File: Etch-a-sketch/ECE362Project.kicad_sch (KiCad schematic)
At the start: 1 part

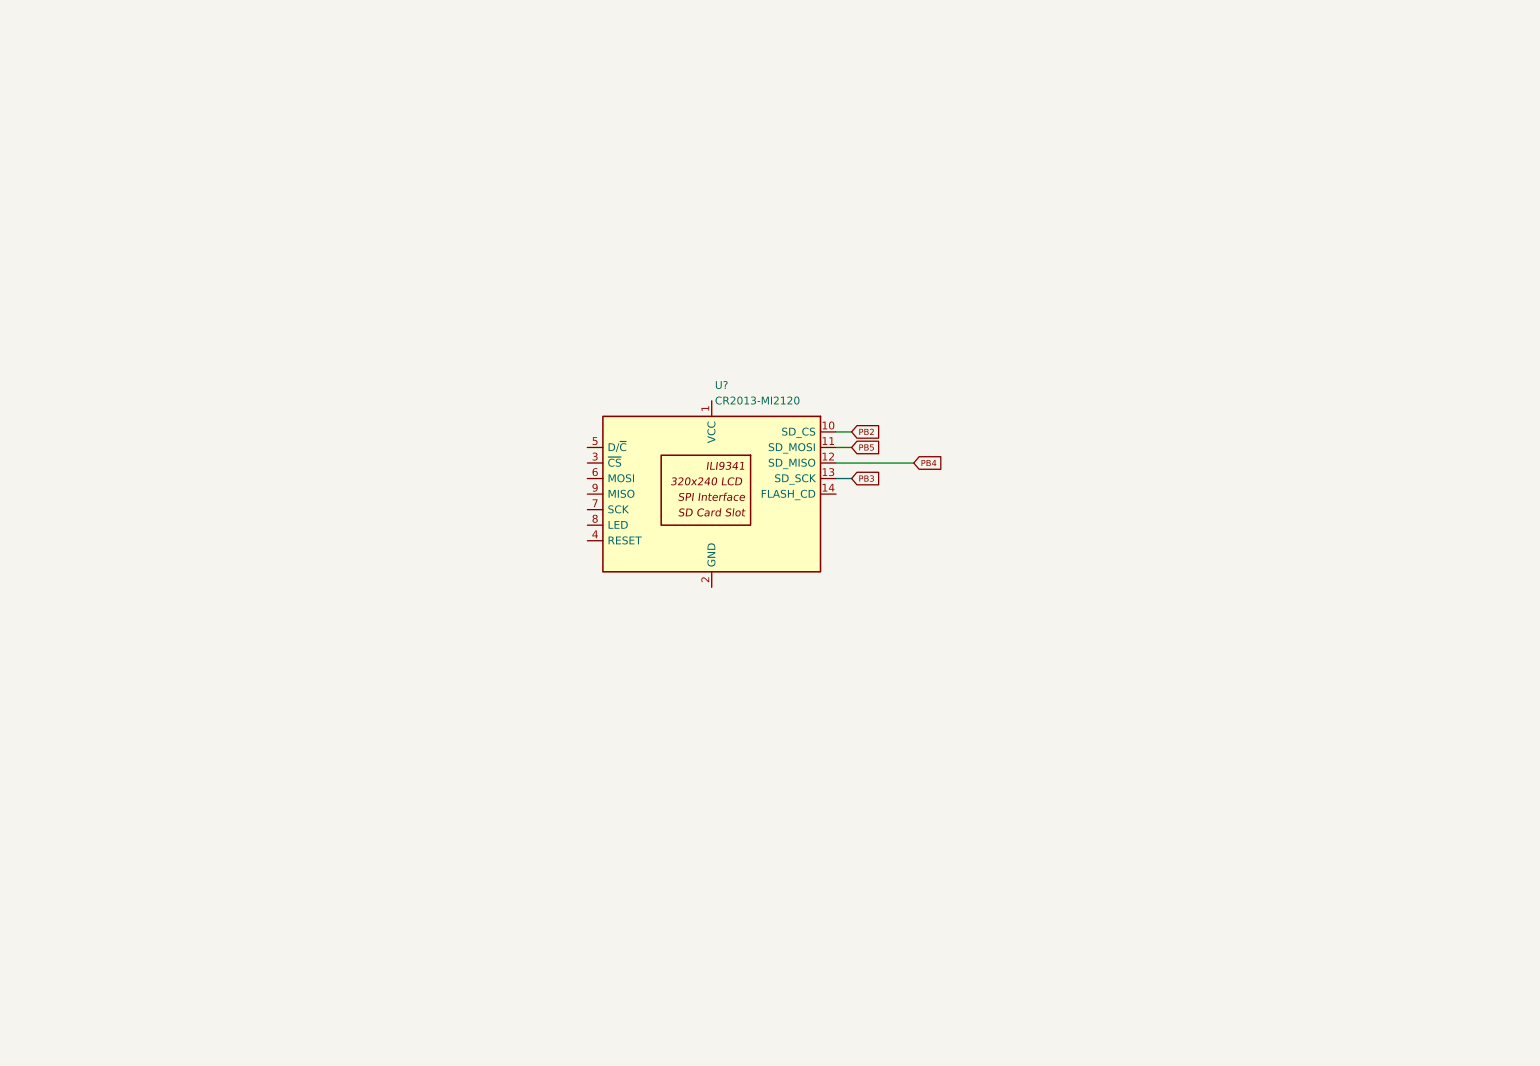
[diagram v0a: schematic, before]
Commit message: finished schematic, should do a schematic review
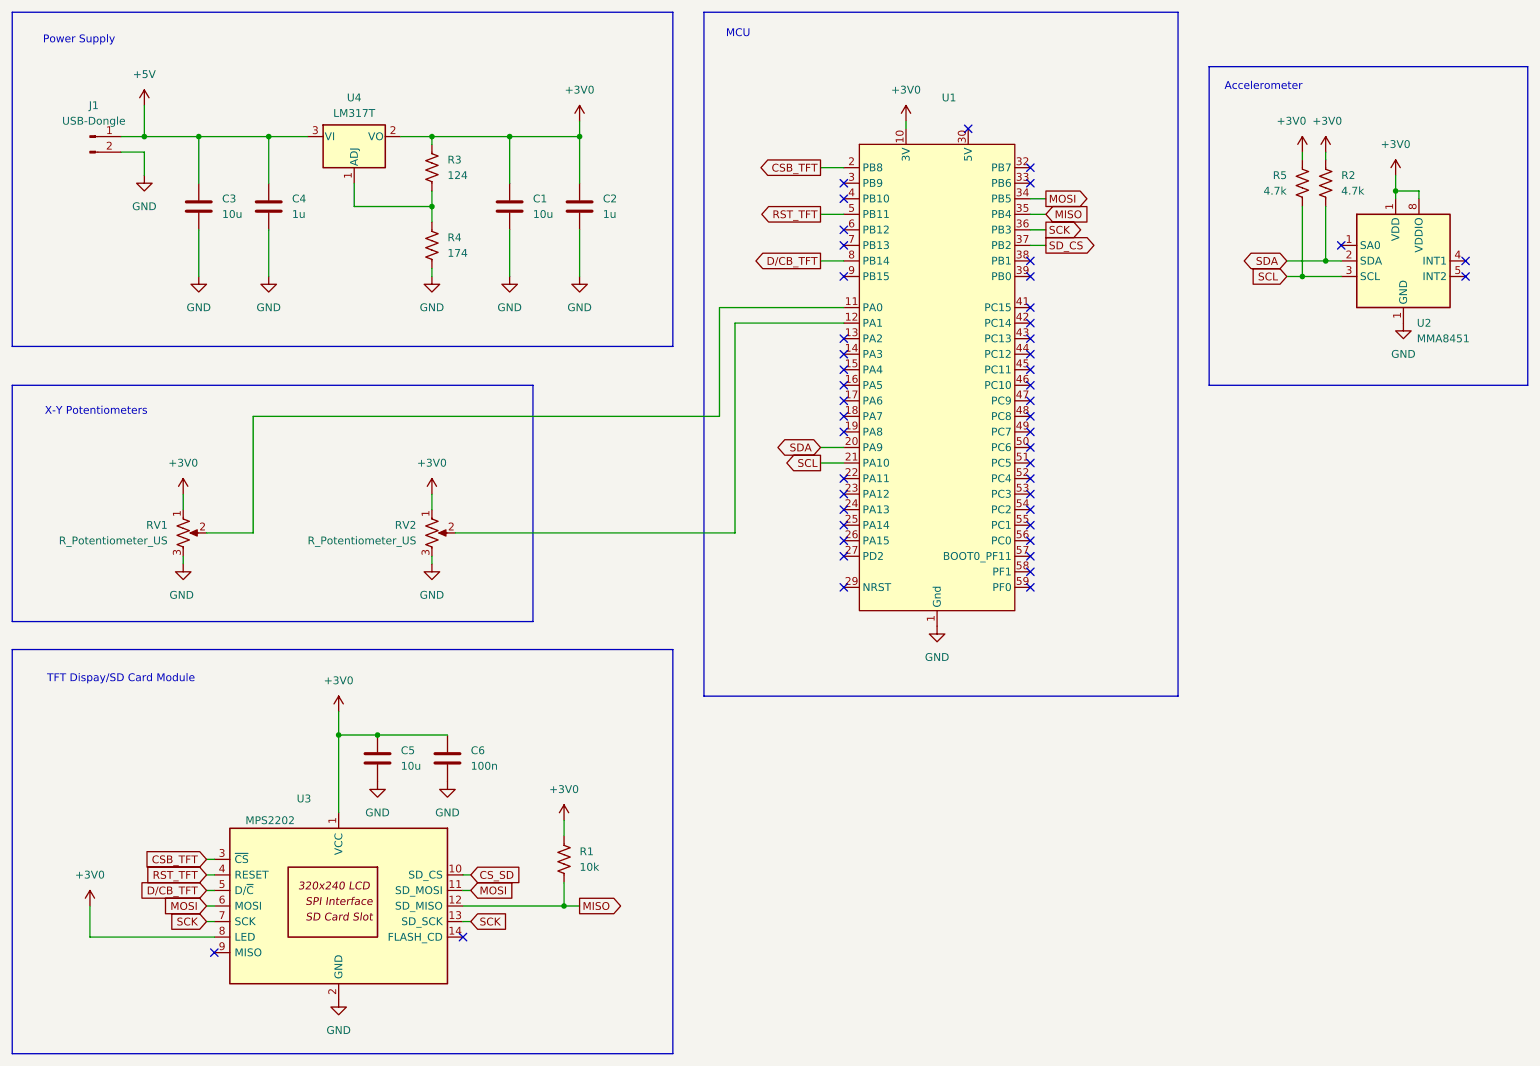
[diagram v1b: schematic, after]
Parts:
- added C1, C3, C5: 10u, symbol Device:C
- added C2, C4: 1u, symbol Device:C
- added C6: 100n, symbol Device:C
- added J1: USB-Dongle, symbol Connector:Conn_01x02_Pin
- added R1: 10k, symbol Device:R_US
- added R2, R5: 4.7k, symbol Device:R_US
- added R3: 124, symbol Device:R_US
- added R4: 174, symbol Device:R_US
- added RV1, RV2: R_Potentiometer_US, symbol Device:R_Potentiometer_US
- added U1: ~, symbol Project_Library:STM32F091_Dev_Board
- added U2: MMA8451, symbol Sensor_Motion:MMA8653FCR1
- added U4: LM317T, symbol Regulator_Linear:LM317_SOT-223
- U3: renamed from U?; value CR2013-MI2120 -> MPS2202
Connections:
- net PB3 is gone; now on net SCK: U3.13 (SD_SCK)
- net PB5 is gone; now on net MOSI: U3.11 (SD_MOSI)
- net +3V0: now reaches U3.1 (VCC)
- net +3V0: now also U3.8 (LED), C1.1, C2.1, C5.1, C6.1, R1.1, R2.1, R3.1, R5.1, RV1.1, RV2.1, U1.10 (3V), U1.40 (3V), U2.1 (VDD), U2.8 (VDDIO), U4.2 (VO)
- net GND: now reaches U3.2 (GND)
- net GND: now also C1.2, C2.2, C3.2, C4.2, C5.2, C6.2, J1.2 (Pin_2), R4.2, RV1.3, RV2.3, U1.1 (Gnd), U1.28 (GND), U1.31 (Gnd), U2.1 (VDD)
- net CSB_TFT: now reaches U3.3 (~{CS})
- net CSB_TFT: now also U1.2 (PB8)
- net RST_TFT: now reaches U3.4 (RESET)
- net RST_TFT: now also U1.5 (PB11)
- net D/CB_TFT: now reaches U3.5 (D/~{C})
- net D/CB_TFT: now also U1.8 (PB14)
- net MOSI: now reaches U3.6 (MOSI)
- net MOSI: now also U1.34 (PB5)
- net SCK: now reaches U3.7 (SCK)
- net SCK: now also U1.36 (PB3)
- net PB2 renamed CS_SD
- net PB4 renamed MISO
- net MISO: now also R1.2, U1.35 (PB4)
- new net: RV1.2, U1.11 (PA0)
- new net: R3.2, R4.1, U4.1 (ADJ)
- new net: RV2.2, U1.12 (PA1)
- new net: U1.30 (5V), U1.60 (5V)
- new net +5V: C3.1, C4.1, J1.1 (Pin_1), U4.3 (VI)
- new net SCL: R5.2, U1.21 (PA10), U2.3 (SCL)
- new net SDA: R2.2, U1.20 (PA9), U2.2 (SDA)
- new net SD_CS: U1.37 (PB2)
- no-connect marks 0 -> 48
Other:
- note added: "Accelerometer"
- note added: "MCU"
- note added: "Power Supply"
- note added: "TFT Dispay/SD Card Module"
- note added: "X-Y Potentiometers"
